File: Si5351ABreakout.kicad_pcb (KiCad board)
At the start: 2 copper layers, 30 x 50 mm, 37 parts, among them J1 Power/Data, J2 SMA-F, J3 SMA-F, J4 SMA-F, J5 CLK0, J6 CLK1, J7 CLK2, T1 TC1-6X+, T2 TC1-6X+, T3 TC1-6X+, U1 Si5351A, X1 ECS-250-8-30B-CKM

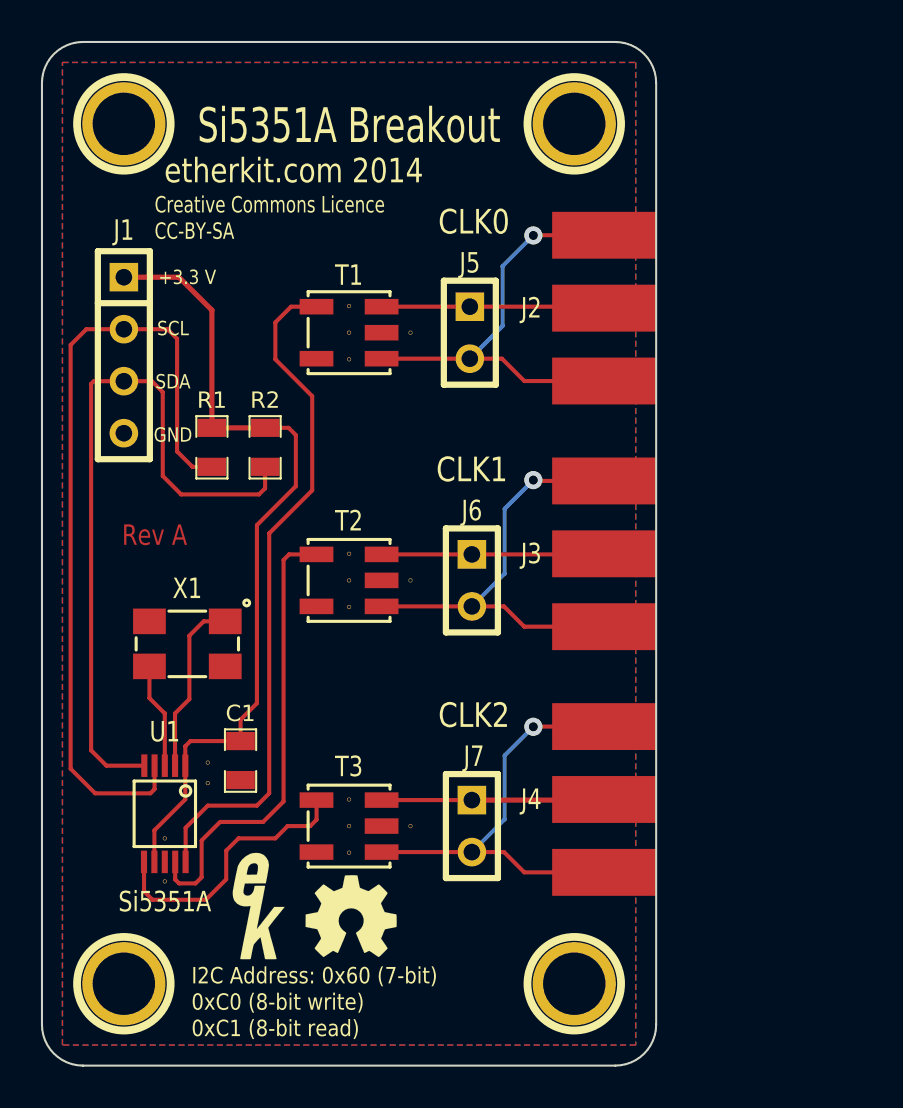
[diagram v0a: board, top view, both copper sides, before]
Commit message: Rev B - I2C level conv, voltage regulator
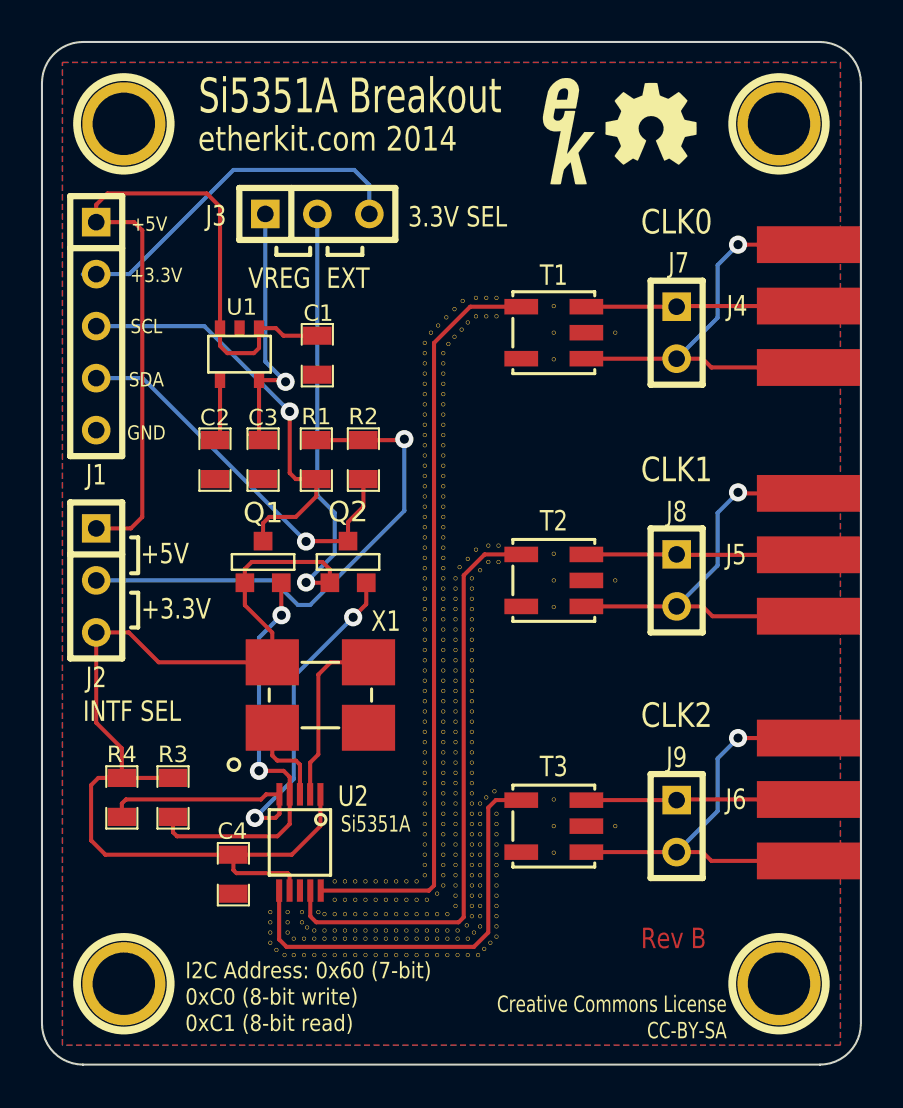
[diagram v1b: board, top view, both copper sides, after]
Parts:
- removed the VIA at (106.0, 91.0)
- added C2: 10n, EtherkitKicadLibrary:SM0805, F.Cu at (108.5, 70.4)
- added C3: 4.7u MLCC, EtherkitKicadLibrary:SM0805, F.Cu at (110.8, 70.4)
- added C4: 100n, EtherkitKicadLibrary:SM0805, F.Cu at (109.3, 90.7)
- added J8: CLK1, EtherkitKicadLibrary:SIL-2, F.Cu at (131.0, 76.3)
- added J9: CLK2, EtherkitKicadLibrary:SIL-2, F.Cu at (131.0, 88.3)
- added Q1: 2N7002, EtherkitKicadLibrary:SOT23-2N7002, F.Cu at (110.8, 75.4)
- added Q2: 2N7002, EtherkitKicadLibrary:SOT23-2N7002, F.Cu at (115.0, 75.4)
- added R3: 10k, EtherkitKicadLibrary:SM0805, F.Cu at (106.4, 86.9)
- added R4: 10k, EtherkitKicadLibrary:SM0805, F.Cu at (103.9, 86.9)
- added U2: Si5351A, EtherkitKicadLibrary:MSOP-10, F.Cu at (112.6, 89.1)
- added VIA: VAL**, EtherkitKicadLibrary:VIA, F.Cu at (114.8, 93.4)
- added VIA: VAL**, EtherkitKicadLibrary:VIA, F.Cu at (115.3, 93.4)
- added VIA: VAL**, EtherkitKicadLibrary:VIA, F.Cu at (115.8, 93.4)
- added VIA: VAL**, EtherkitKicadLibrary:VIA, F.Cu at (116.3, 93.4)
- added VIA: VAL**, EtherkitKicadLibrary:VIA, F.Cu at (116.8, 93.4)
- added VIA: VAL**, EtherkitKicadLibrary:VIA, F.Cu at (117.3, 93.4)
- added VIA: VAL**, EtherkitKicadLibrary:VIA, F.Cu at (117.8, 93.4)
- added VIA: VAL**, EtherkitKicadLibrary:VIA, F.Cu at (118.3, 93.4)
- added VIA: VAL**, EtherkitKicadLibrary:VIA, F.Cu at (118.8, 93.4)
- added VIA: VAL**, EtherkitKicadLibrary:VIA, F.Cu at (119.3, 93.4)
- added VIA: VAL**, EtherkitKicadLibrary:VIA, F.Cu at (119.8, 93.4)
- added VIA: VAL**, EtherkitKicadLibrary:VIA, F.Cu at (120.3, 93.4)
- added VIA: VAL**, EtherkitKicadLibrary:VIA, F.Cu at (121.0, 92.7)
- added VIA: VAL**, EtherkitKicadLibrary:VIA, F.Cu at (120.8, 93.2)
- added VIA: VAL**, EtherkitKicadLibrary:VIA, F.Cu at (121.0, 92.2)
- added VIA: VAL**, EtherkitKicadLibrary:VIA, F.Cu at (121.0, 91.7)
- added VIA: VAL**, EtherkitKicadLibrary:VIA, F.Cu at (121.0, 91.2)
- added VIA: VAL**, EtherkitKicadLibrary:VIA, F.Cu at (121.0, 90.7)
- added VIA: VAL**, EtherkitKicadLibrary:VIA, F.Cu at (121.0, 90.2)
- added VIA: VAL**, EtherkitKicadLibrary:VIA, F.Cu at (121.0, 89.7)
- added VIA: VAL**, EtherkitKicadLibrary:VIA, F.Cu at (121.0, 89.2)
- added VIA: VAL**, EtherkitKicadLibrary:VIA, F.Cu at (121.0, 88.7)
- added VIA: VAL**, EtherkitKicadLibrary:VIA, F.Cu at (121.0, 88.2)
- added VIA: VAL**, EtherkitKicadLibrary:VIA, F.Cu at (121.0, 87.7)
- added VIA: VAL**, EtherkitKicadLibrary:VIA, F.Cu at (121.0, 87.2)
- added VIA: VAL**, EtherkitKicadLibrary:VIA, F.Cu at (121.0, 86.7)
- added VIA: VAL**, EtherkitKicadLibrary:VIA, F.Cu at (121.0, 86.2)
- added VIA: VAL**, EtherkitKicadLibrary:VIA, F.Cu at (121.0, 85.7)
- added VIA: VAL**, EtherkitKicadLibrary:VIA, F.Cu at (121.0, 85.2)
- added VIA: VAL**, EtherkitKicadLibrary:VIA, F.Cu at (121.0, 84.7)
- added VIA: VAL**, EtherkitKicadLibrary:VIA, F.Cu at (121.0, 84.2)
- added VIA: VAL**, EtherkitKicadLibrary:VIA, F.Cu at (121.0, 83.7)
- added VIA: VAL**, EtherkitKicadLibrary:VIA, F.Cu at (121.0, 83.2)
- added VIA: VAL**, EtherkitKicadLibrary:VIA, F.Cu at (121.0, 82.7)
- added VIA: VAL**, EtherkitKicadLibrary:VIA, F.Cu at (121.0, 82.2)
- added VIA: VAL**, EtherkitKicadLibrary:VIA, F.Cu at (121.0, 81.7)
- added VIA: VAL**, EtherkitKicadLibrary:VIA, F.Cu at (121.0, 81.2)
- added VIA: VAL**, EtherkitKicadLibrary:VIA, F.Cu at (121.0, 80.7)
- added VIA: VAL**, EtherkitKicadLibrary:VIA, F.Cu at (121.0, 80.2)
- added VIA: VAL**, EtherkitKicadLibrary:VIA, F.Cu at (121.0, 79.7)
- added VIA: VAL**, EtherkitKicadLibrary:VIA, F.Cu at (121.0, 79.2)
- added VIA: VAL**, EtherkitKicadLibrary:VIA, F.Cu at (121.0, 78.7)
- added VIA: VAL**, EtherkitKicadLibrary:VIA, F.Cu at (121.0, 78.2)
- added VIA: VAL**, EtherkitKicadLibrary:VIA, F.Cu at (121.0, 77.7)
- added VIA: VAL**, EtherkitKicadLibrary:VIA, F.Cu at (121.0, 77.2)
- added VIA: VAL**, EtherkitKicadLibrary:VIA, F.Cu at (121.0, 76.7)
- added VIA: VAL**, EtherkitKicadLibrary:VIA, F.Cu at (121.0, 76.2)
- added VIA: VAL**, EtherkitKicadLibrary:VIA, F.Cu at (121.8, 75.4)
- added VIA: VAL**, EtherkitKicadLibrary:VIA, F.Cu at (122.3, 75.4)
- added VIA: VAL**, EtherkitKicadLibrary:VIA, F.Cu at (121.4, 75.8)
- added VIA: VAL**, EtherkitKicadLibrary:VIA, F.Cu at (114.3, 92.6)
- added VIA: VAL**, EtherkitKicadLibrary:VIA, F.Cu at (114.8, 92.6)
- added VIA: VAL**, EtherkitKicadLibrary:VIA, F.Cu at (115.3, 92.6)
- added VIA: VAL**, EtherkitKicadLibrary:VIA, F.Cu at (115.8, 92.6)
- added VIA: VAL**, EtherkitKicadLibrary:VIA, F.Cu at (116.3, 92.6)
- added VIA: VAL**, EtherkitKicadLibrary:VIA, F.Cu at (116.8, 92.6)
- added VIA: VAL**, EtherkitKicadLibrary:VIA, F.Cu at (117.3, 92.6)
- added VIA: VAL**, EtherkitKicadLibrary:VIA, F.Cu at (117.8, 92.6)
- added VIA: VAL**, EtherkitKicadLibrary:VIA, F.Cu at (118.3, 92.6)
- added VIA: VAL**, EtherkitKicadLibrary:VIA, F.Cu at (118.8, 92.6)
- added VIA: VAL**, EtherkitKicadLibrary:VIA, F.Cu at (112.0, 92.5)
- added VIA: VAL**, EtherkitKicadLibrary:VIA, F.Cu at (119.3, 92.6)
- added VIA: VAL**, EtherkitKicadLibrary:VIA, F.Cu at (119.8, 92.6)
- added VIA: VAL**, EtherkitKicadLibrary:VIA, F.Cu at (120.2, 92.2)
- added VIA: VAL**, EtherkitKicadLibrary:VIA, F.Cu at (120.2, 91.7)
- added VIA: VAL**, EtherkitKicadLibrary:VIA, F.Cu at (120.2, 91.2)
- added VIA: VAL**, EtherkitKicadLibrary:VIA, F.Cu at (120.2, 90.7)
- added VIA: VAL**, EtherkitKicadLibrary:VIA, F.Cu at (120.2, 90.2)
- added VIA: VAL**, EtherkitKicadLibrary:VIA, F.Cu at (120.2, 89.7)
- added VIA: VAL**, EtherkitKicadLibrary:VIA, F.Cu at (120.2, 89.2)
- added VIA: VAL**, EtherkitKicadLibrary:VIA, F.Cu at (120.2, 88.7)
- added VIA: VAL**, EtherkitKicadLibrary:VIA, F.Cu at (112.0, 93.0)
- added VIA: VAL**, EtherkitKicadLibrary:VIA, F.Cu at (120.2, 88.2)
- added VIA: VAL**, EtherkitKicadLibrary:VIA, F.Cu at (120.2, 87.7)
- added VIA: VAL**, EtherkitKicadLibrary:VIA, F.Cu at (120.2, 87.2)
- added VIA: VAL**, EtherkitKicadLibrary:VIA, F.Cu at (120.2, 86.7)
- added VIA: VAL**, EtherkitKicadLibrary:VIA, F.Cu at (120.2, 86.2)
- added VIA: VAL**, EtherkitKicadLibrary:VIA, F.Cu at (120.2, 85.7)
- added VIA: VAL**, EtherkitKicadLibrary:VIA, F.Cu at (120.2, 85.2)
- added VIA: VAL**, EtherkitKicadLibrary:VIA, F.Cu at (120.2, 84.7)
- added VIA: VAL**, EtherkitKicadLibrary:VIA, F.Cu at (120.2, 84.2)
- added VIA: VAL**, EtherkitKicadLibrary:VIA, F.Cu at (120.2, 83.7)
- added VIA: VAL**, EtherkitKicadLibrary:VIA, F.Cu at (111.2, 93.0)
- added VIA: VAL**, EtherkitKicadLibrary:VIA, F.Cu at (120.2, 83.2)
- added VIA: VAL**, EtherkitKicadLibrary:VIA, F.Cu at (120.2, 82.7)
- added VIA: VAL**, EtherkitKicadLibrary:VIA, F.Cu at (120.2, 82.2)
- added VIA: VAL**, EtherkitKicadLibrary:VIA, F.Cu at (120.2, 81.7)
- added VIA: VAL**, EtherkitKicadLibrary:VIA, F.Cu at (120.2, 81.2)
- added VIA: VAL**, EtherkitKicadLibrary:VIA, F.Cu at (120.2, 80.7)
- added VIA: VAL**, EtherkitKicadLibrary:VIA, F.Cu at (120.2, 80.2)
- added VIA: VAL**, EtherkitKicadLibrary:VIA, F.Cu at (120.2, 79.7)
- added VIA: VAL**, EtherkitKicadLibrary:VIA, F.Cu at (120.2, 79.2)
- added VIA: VAL**, EtherkitKicadLibrary:VIA, F.Cu at (120.2, 78.7)
- added VIA: VAL**, EtherkitKicadLibrary:VIA, F.Cu at (112.0, 93.5)
- added VIA: VAL**, EtherkitKicadLibrary:VIA, F.Cu at (120.2, 78.2)
- added VIA: VAL**, EtherkitKicadLibrary:VIA, F.Cu at (120.2, 77.7)
- added VIA: VAL**, EtherkitKicadLibrary:VIA, F.Cu at (120.2, 77.2)
- added VIA: VAL**, EtherkitKicadLibrary:VIA, F.Cu at (120.2, 76.7)
- added VIA: VAL**, EtherkitKicadLibrary:VIA, F.Cu at (120.2, 76.2)
- added VIA: VAL**, EtherkitKicadLibrary:VIA, F.Cu at (121.8, 74.6)
- added VIA: VAL**, EtherkitKicadLibrary:VIA, F.Cu at (122.3, 74.6)
- added VIA: VAL**, EtherkitKicadLibrary:VIA, F.Cu at (120.4, 75.7)
- added VIA: VAL**, EtherkitKicadLibrary:VIA, F.Cu at (121.2, 74.8)
- added VIA: VAL**, EtherkitKicadLibrary:VIA, F.Cu at (120.8, 75.2)
- added VIA: VAL**, EtherkitKicadLibrary:VIA, F.Cu at (111.2, 93.5)
- added VIA: VAL**, EtherkitKicadLibrary:VIA, F.Cu at (114.3, 91.9)
- added VIA: VAL**, EtherkitKicadLibrary:VIA, F.Cu at (114.3, 91.0)
- added VIA: VAL**, EtherkitKicadLibrary:VIA, F.Cu at (114.8, 91.9)
- added VIA: VAL**, EtherkitKicadLibrary:VIA, F.Cu at (115.3, 91.9)
- added VIA: VAL**, EtherkitKicadLibrary:VIA, F.Cu at (115.8, 91.9)
- added VIA: VAL**, EtherkitKicadLibrary:VIA, F.Cu at (116.3, 91.9)
- added VIA: VAL**, EtherkitKicadLibrary:VIA, F.Cu at (116.8, 91.9)
- added VIA: VAL**, EtherkitKicadLibrary:VIA, F.Cu at (117.3, 91.9)
- added VIA: VAL**, EtherkitKicadLibrary:VIA, F.Cu at (117.8, 91.9)
- added VIA: VAL**, EtherkitKicadLibrary:VIA, F.Cu at (118.3, 91.9)
- added VIA: VAL**, EtherkitKicadLibrary:VIA, F.Cu at (111.5, 94.3)
- added VIA: VAL**, EtherkitKicadLibrary:VIA, F.Cu at (118.8, 91.9)
- added VIA: VAL**, EtherkitKicadLibrary:VIA, F.Cu at (119.6, 90.7)
- added VIA: VAL**, EtherkitKicadLibrary:VIA, F.Cu at (114.8, 91.0)
- added VIA: VAL**, EtherkitKicadLibrary:VIA, F.Cu at (115.3, 91.0)
- added VIA: VAL**, EtherkitKicadLibrary:VIA, F.Cu at (115.8, 91.0)
- added VIA: VAL**, EtherkitKicadLibrary:VIA, F.Cu at (116.3, 91.0)
- added VIA: VAL**, EtherkitKicadLibrary:VIA, F.Cu at (116.8, 91.0)
- added VIA: VAL**, EtherkitKicadLibrary:VIA, F.Cu at (117.3, 91.0)
- added VIA: VAL**, EtherkitKicadLibrary:VIA, F.Cu at (117.8, 91.0)
- added VIA: VAL**, EtherkitKicadLibrary:VIA, F.Cu at (118.3, 91.0)
- added VIA: VAL**, EtherkitKicadLibrary:VIA, F.Cu at (112.3, 93.8)
- added VIA: VAL**, EtherkitKicadLibrary:VIA, F.Cu at (118.7, 90.7)
- added VIA: VAL**, EtherkitKicadLibrary:VIA, F.Cu at (119.6, 91.2)
- added VIA: VAL**, EtherkitKicadLibrary:VIA, F.Cu at (119.3, 91.6)
- added VIA: VAL**, EtherkitKicadLibrary:VIA, F.Cu at (119.6, 90.2)
- added VIA: VAL**, EtherkitKicadLibrary:VIA, F.Cu at (119.6, 89.7)
- added VIA: VAL**, EtherkitKicadLibrary:VIA, F.Cu at (119.6, 89.2)
- added VIA: VAL**, EtherkitKicadLibrary:VIA, F.Cu at (119.6, 88.7)
- added VIA: VAL**, EtherkitKicadLibrary:VIA, F.Cu at (119.6, 88.2)
- added VIA: VAL**, EtherkitKicadLibrary:VIA, F.Cu at (119.6, 87.7)
- added VIA: VAL**, EtherkitKicadLibrary:VIA, F.Cu at (119.6, 87.2)
- added VIA: VAL**, EtherkitKicadLibrary:VIA, F.Cu at (112.8, 94.6)
- added VIA: VAL**, EtherkitKicadLibrary:VIA, F.Cu at (119.6, 86.7)
- added VIA: VAL**, EtherkitKicadLibrary:VIA, F.Cu at (119.6, 86.2)
- added VIA: VAL**, EtherkitKicadLibrary:VIA, F.Cu at (119.6, 85.7)
- added VIA: VAL**, EtherkitKicadLibrary:VIA, F.Cu at (119.6, 85.2)
- added VIA: VAL**, EtherkitKicadLibrary:VIA, F.Cu at (119.6, 84.7)
- added VIA: VAL**, EtherkitKicadLibrary:VIA, F.Cu at (119.6, 84.2)
- added VIA: VAL**, EtherkitKicadLibrary:VIA, F.Cu at (119.6, 83.7)
- added VIA: VAL**, EtherkitKicadLibrary:VIA, F.Cu at (119.6, 83.2)
- added VIA: VAL**, EtherkitKicadLibrary:VIA, F.Cu at (119.6, 82.7)
- added VIA: VAL**, EtherkitKicadLibrary:VIA, F.Cu at (119.6, 82.2)
- added VIA: VAL**, EtherkitKicadLibrary:VIA, F.Cu at (112.3, 94.6)
- added VIA: VAL**, EtherkitKicadLibrary:VIA, F.Cu at (119.6, 81.7)
- added VIA: VAL**, EtherkitKicadLibrary:VIA, F.Cu at (119.6, 81.2)
- added VIA: VAL**, EtherkitKicadLibrary:VIA, F.Cu at (119.6, 80.7)
- added VIA: VAL**, EtherkitKicadLibrary:VIA, F.Cu at (119.6, 80.2)
- added VIA: VAL**, EtherkitKicadLibrary:VIA, F.Cu at (119.6, 79.7)
- added VIA: VAL**, EtherkitKicadLibrary:VIA, F.Cu at (119.6, 79.2)
- added VIA: VAL**, EtherkitKicadLibrary:VIA, F.Cu at (119.6, 78.7)
- added VIA: VAL**, EtherkitKicadLibrary:VIA, F.Cu at (119.6, 78.2)
- added VIA: VAL**, EtherkitKicadLibrary:VIA, F.Cu at (119.6, 77.7)
- added VIA: VAL**, EtherkitKicadLibrary:VIA, F.Cu at (119.6, 77.2)
- added VIA: VAL**, EtherkitKicadLibrary:VIA, F.Cu at (111.2, 94.0)
- added VIA: VAL**, EtherkitKicadLibrary:VIA, F.Cu at (119.6, 76.7)
- added VIA: VAL**, EtherkitKicadLibrary:VIA, F.Cu at (119.6, 76.2)
- added VIA: VAL**, EtherkitKicadLibrary:VIA, F.Cu at (119.6, 75.7)
- added VIA: VAL**, EtherkitKicadLibrary:VIA, F.Cu at (119.6, 75.2)
- added VIA: VAL**, EtherkitKicadLibrary:VIA, F.Cu at (119.6, 74.7)
- added VIA: VAL**, EtherkitKicadLibrary:VIA, F.Cu at (119.6, 74.2)
- added VIA: VAL**, EtherkitKicadLibrary:VIA, F.Cu at (119.6, 73.7)
- added VIA: VAL**, EtherkitKicadLibrary:VIA, F.Cu at (119.6, 73.2)
- added VIA: VAL**, EtherkitKicadLibrary:VIA, F.Cu at (119.6, 72.7)
- added VIA: VAL**, EtherkitKicadLibrary:VIA, F.Cu at (119.6, 72.2)
- added VIA: VAL**, EtherkitKicadLibrary:VIA, F.Cu at (111.8, 94.6)
- added VIA: VAL**, EtherkitKicadLibrary:VIA, F.Cu at (119.6, 71.7)
- added VIA: VAL**, EtherkitKicadLibrary:VIA, F.Cu at (119.6, 71.2)
- added VIA: VAL**, EtherkitKicadLibrary:VIA, F.Cu at (119.6, 70.7)
- added VIA: VAL**, EtherkitKicadLibrary:VIA, F.Cu at (119.6, 70.2)
- added VIA: VAL**, EtherkitKicadLibrary:VIA, F.Cu at (119.6, 69.7)
- added VIA: VAL**, EtherkitKicadLibrary:VIA, F.Cu at (119.6, 69.2)
- added VIA: VAL**, EtherkitKicadLibrary:VIA, F.Cu at (119.6, 68.7)
- added VIA: VAL**, EtherkitKicadLibrary:VIA, F.Cu at (119.6, 68.2)
- added VIA: VAL**, EtherkitKicadLibrary:VIA, F.Cu at (119.6, 67.7)
- added VIA: VAL**, EtherkitKicadLibrary:VIA, F.Cu at (119.6, 67.2)
- added VIA: VAL**, EtherkitKicadLibrary:VIA, F.Cu at (112.8, 93.8)
- added VIA: VAL**, EtherkitKicadLibrary:VIA, F.Cu at (119.6, 66.7)
- added VIA: VAL**, EtherkitKicadLibrary:VIA, F.Cu at (119.6, 66.2)
- added VIA: VAL**, EtherkitKicadLibrary:VIA, F.Cu at (119.6, 65.7)
- added VIA: VAL**, EtherkitKicadLibrary:VIA, F.Cu at (119.6, 65.2)
- added VIA: VAL**, EtherkitKicadLibrary:VIA, F.Cu at (121.2, 63.4)
- added VIA: VAL**, EtherkitKicadLibrary:VIA, F.Cu at (121.7, 63.4)
- added VIA: VAL**, EtherkitKicadLibrary:VIA, F.Cu at (122.2, 63.4)
- added VIA: VAL**, EtherkitKicadLibrary:VIA, F.Cu at (119.8, 64.8)
- added VIA: VAL**, EtherkitKicadLibrary:VIA, F.Cu at (120.2, 64.4)
- added VIA: VAL**, EtherkitKicadLibrary:VIA, F.Cu at (120.5, 64.0)
- added VIA: VAL**, EtherkitKicadLibrary:VIA, F.Cu at (113.3, 93.8)
- added VIA: VAL**, EtherkitKicadLibrary:VIA, F.Cu at (120.8, 63.7)
- added VIA: VAL**, EtherkitKicadLibrary:VIA, F.Cu at (118.7, 90.2)
- added VIA: VAL**, EtherkitKicadLibrary:VIA, F.Cu at (118.7, 89.7)
- added VIA: VAL**, EtherkitKicadLibrary:VIA, F.Cu at (118.7, 89.2)
- added VIA: VAL**, EtherkitKicadLibrary:VIA, F.Cu at (118.7, 88.7)
- added VIA: VAL**, EtherkitKicadLibrary:VIA, F.Cu at (118.7, 88.2)
- added VIA: VAL**, EtherkitKicadLibrary:VIA, F.Cu at (118.7, 87.7)
- added VIA: VAL**, EtherkitKicadLibrary:VIA, F.Cu at (118.7, 87.2)
- added VIA: VAL**, EtherkitKicadLibrary:VIA, F.Cu at (118.7, 86.7)
- added VIA: VAL**, EtherkitKicadLibrary:VIA, F.Cu at (118.7, 86.2)
- added VIA: VAL**, EtherkitKicadLibrary:VIA, F.Cu at (113.8, 93.8)
- added VIA: VAL**, EtherkitKicadLibrary:VIA, F.Cu at (118.7, 85.7)
- added VIA: VAL**, EtherkitKicadLibrary:VIA, F.Cu at (118.7, 85.2)
- added VIA: VAL**, EtherkitKicadLibrary:VIA, F.Cu at (118.7, 84.7)
- added VIA: VAL**, EtherkitKicadLibrary:VIA, F.Cu at (118.7, 84.2)
- added VIA: VAL**, EtherkitKicadLibrary:VIA, F.Cu at (118.7, 83.7)
- added VIA: VAL**, EtherkitKicadLibrary:VIA, F.Cu at (118.7, 83.2)
- added VIA: VAL**, EtherkitKicadLibrary:VIA, F.Cu at (118.7, 82.7)
- added VIA: VAL**, EtherkitKicadLibrary:VIA, F.Cu at (118.7, 82.2)
- added VIA: VAL**, EtherkitKicadLibrary:VIA, F.Cu at (118.7, 81.7)
- added VIA: VAL**, EtherkitKicadLibrary:VIA, F.Cu at (118.7, 81.2)
- added VIA: VAL**, EtherkitKicadLibrary:VIA, F.Cu at (114.3, 93.8)
- added VIA: VAL**, EtherkitKicadLibrary:VIA, F.Cu at (118.7, 80.7)
- added VIA: VAL**, EtherkitKicadLibrary:VIA, F.Cu at (118.7, 80.2)
- added VIA: VAL**, EtherkitKicadLibrary:VIA, F.Cu at (118.7, 79.7)
- added VIA: VAL**, EtherkitKicadLibrary:VIA, F.Cu at (118.7, 79.2)
- added VIA: VAL**, EtherkitKicadLibrary:VIA, F.Cu at (118.7, 78.7)
- added VIA: VAL**, EtherkitKicadLibrary:VIA, F.Cu at (118.7, 78.2)
- added VIA: VAL**, EtherkitKicadLibrary:VIA, F.Cu at (118.7, 77.7)
- added VIA: VAL**, EtherkitKicadLibrary:VIA, F.Cu at (118.7, 77.2)
- added VIA: VAL**, EtherkitKicadLibrary:VIA, F.Cu at (118.7, 76.7)
- added VIA: VAL**, EtherkitKicadLibrary:VIA, F.Cu at (118.7, 76.2)
- added VIA: VAL**, EtherkitKicadLibrary:VIA, F.Cu at (114.8, 93.8)
- added VIA: VAL**, EtherkitKicadLibrary:VIA, F.Cu at (118.7, 75.7)
- added VIA: VAL**, EtherkitKicadLibrary:VIA, F.Cu at (118.7, 75.2)
- added VIA: VAL**, EtherkitKicadLibrary:VIA, F.Cu at (118.7, 74.7)
- added VIA: VAL**, EtherkitKicadLibrary:VIA, F.Cu at (118.7, 74.2)
- added VIA: VAL**, EtherkitKicadLibrary:VIA, F.Cu at (118.7, 73.7)
- added VIA: VAL**, EtherkitKicadLibrary:VIA, F.Cu at (118.7, 73.2)
- added VIA: VAL**, EtherkitKicadLibrary:VIA, F.Cu at (118.7, 72.7)
- added VIA: VAL**, EtherkitKicadLibrary:VIA, F.Cu at (118.7, 72.2)
- added VIA: VAL**, EtherkitKicadLibrary:VIA, F.Cu at (118.7, 71.7)
- added VIA: VAL**, EtherkitKicadLibrary:VIA, F.Cu at (118.7, 71.2)
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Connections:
- C1 pad 1: +3.3V -> +5V
- J1 pad 1: +3.3V -> +5V
- J1 pad 2: Net-(J1-Pad2) -> +3.3V
- J1 pad 4: GND -> Net-(J1-Pad4)
- J2 pad 1: Net-(J2-Pad1) -> +5V
- J3 pad 1: Net-(J3-Pad1) -> Net-(C3-Pad1)
- J3 pad 2: Net-(J3-Pad2) -> +3.3VREG
- J5 pad 1: Net-(J2-Pad1) -> Net-(J5-Pad1)
- J5 pad 2: Net-(J2-Pad2) -> Net-(J5-Pad2)
- J6 pad 1: Net-(J3-Pad1) -> Net-(J6-Pad1)
- J6 pad 2: Net-(J3-Pad2) -> Net-(J6-Pad2)
- R1 pad 1: +3.3V -> Net-(J2-Pad2)
- R1 pad 2: Net-(J1-Pad2) -> Net-(J1-Pad3)
- R2 pad 1: +3.3V -> Net-(J2-Pad2)
- R2 pad 2: Net-(J1-Pad3) -> Net-(J1-Pad4)
- T1 pad 1: Net-(J2-Pad1) -> Net-(J4-Pad1)
- T1 pad 2: GND -> (no net)
- T1 pad 3: Net-(J2-Pad2) -> Net-(J4-Pad2)
- T2 pad 1: Net-(J3-Pad1) -> Net-(J5-Pad1)
- T2 pad 2: GND -> (no net)
- T2 pad 3: Net-(J3-Pad2) -> Net-(J5-Pad2)
- T3 pad 1: Net-(J4-Pad1) -> Net-(J6-Pad1)
- T3 pad 2: GND -> (no net)
- T3 pad 3: Net-(J4-Pad2) -> Net-(J6-Pad2)
- U1 pad 1: +3.3V -> +5V
- U1 pad 2: Net-(U1-Pad2) -> GND
- U1 pad 3: Net-(U1-Pad3) -> +5V
- U1 pad 4: Net-(J1-Pad2) -> Net-(C2-Pad1)
- U1 pad 5: Net-(J1-Pad3) -> Net-(C3-Pad1)
- X1 pad 1: Net-(U1-Pad2) -> Net-(U2-Pad3)
- X1 pad 2: (no net) -> GND
- X1 pad 3: Net-(U1-Pad3) -> Net-(U2-Pad2)
- X1 pad 4: (no net) -> +3.3VREG
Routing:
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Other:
- board size 30 x 50 mm -> 40 x 50 mm
- net class Default: clearance 0.2 -> 0.15
- rule trace_clearance: 0.2 -> 0.15
- board text added: "+3.3V"
- board text added: "+5V"
- board text added: "3.3V SEL"
- board text added: "Creative Commons License CC-BY-SA"
- board text added: "EXT"
- board text added: "INTF SEL"
- board text added: "Rev B"
- board text added: "VREG"
- board text removed: "+3.3 V"
- board text removed: "Creative Commons Licence CC-BY-SA"
- board text removed: "Rev A"

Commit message: Rev C updates
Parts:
- removed T1, T2, T3: Mini-Circuits TC1-6X+, EtherkitKicadLibrary:TC1-6X+
- removed the VIA at (111.2, 92.5)
- removed the VIA at (125.0, 75.0)
- removed the VIA at (114.8, 93.4)
- removed the VIA at (115.3, 93.4)
- removed the VIA at (115.8, 93.4)
- removed the VIA at (116.3, 93.4)
- removed the VIA at (116.8, 93.4)
- removed the VIA at (117.3, 93.4)
- removed the VIA at (117.8, 93.4)
- removed the VIA at (118.3, 93.4)
- removed the VIA at (118.8, 93.4)
- removed the VIA at (119.3, 93.4)
- removed the VIA at (125.0, 77.6)
- removed the VIA at (119.8, 93.4)
- removed the VIA at (120.3, 93.4)
- removed the VIA at (121.0, 92.7)
- removed the VIA at (120.8, 93.2)
- removed the VIA at (121.0, 92.2)
- removed the VIA at (121.0, 91.7)
- removed the VIA at (121.0, 91.2)
- removed the VIA at (121.0, 90.7)
- removed the VIA at (121.0, 90.2)
- removed the VIA at (121.0, 89.7)
- removed the VIA at (128.0, 64.2)
- removed the VIA at (121.0, 89.2)
- removed the VIA at (121.0, 88.7)
- removed the VIA at (121.0, 88.2)
- removed the VIA at (121.0, 87.7)
- removed the VIA at (121.0, 87.2)
- removed the VIA at (121.0, 86.7)
- removed the VIA at (121.0, 86.2)
- removed the VIA at (121.0, 85.7)
- removed the VIA at (121.0, 85.2)
- removed the VIA at (121.0, 84.7)
- removed the VIA at (125.0, 64.2)
- removed the VIA at (121.0, 84.2)
- removed the VIA at (121.0, 83.7)
- removed the VIA at (121.0, 83.2)
- removed the VIA at (121.0, 82.7)
- removed the VIA at (121.0, 82.2)
- removed the VIA at (121.0, 81.7)
- removed the VIA at (121.0, 81.2)
- removed the VIA at (121.0, 80.7)
- removed the VIA at (121.0, 80.2)
- removed the VIA at (121.0, 79.7)
- removed the VIA at (125.0, 65.5)
- removed the VIA at (121.0, 79.2)
- removed the VIA at (121.0, 78.7)
- removed the VIA at (121.0, 78.2)
- removed the VIA at (121.0, 77.7)
- removed the VIA at (121.0, 77.2)
- removed the VIA at (121.0, 76.7)
- removed the VIA at (121.0, 76.2)
- removed the VIA at (121.8, 75.4)
- removed the VIA at (122.3, 75.4)
- removed the VIA at (121.4, 75.8)
- removed the VIA at (125.0, 62.9)
- removed the VIA at (114.3, 92.6)
- removed the VIA at (114.8, 92.6)
- removed the VIA at (115.3, 92.6)
- removed the VIA at (115.8, 92.6)
- removed the VIA at (116.3, 92.6)
- removed the VIA at (116.8, 92.6)
- removed the VIA at (117.3, 92.6)
- removed the VIA at (117.8, 92.6)
- removed the VIA at (118.3, 92.6)
- removed the VIA at (118.8, 92.6)
- removed the VIA at (112.0, 92.5)
- removed the VIA at (119.3, 92.6)
- removed the VIA at (119.8, 92.6)
- removed the VIA at (120.2, 92.2)
- removed the VIA at (120.2, 91.7)
- removed the VIA at (120.2, 91.2)
- removed the VIA at (120.2, 90.7)
- removed the VIA at (120.2, 90.2)
- removed the VIA at (120.2, 89.7)
- removed the VIA at (120.2, 89.2)
- removed the VIA at (120.2, 88.7)
- removed the VIA at (112.0, 93.0)
- removed the VIA at (120.2, 88.2)
- removed the VIA at (120.2, 87.7)
- removed the VIA at (120.2, 87.2)
- removed the VIA at (120.2, 86.7)
- removed the VIA at (120.2, 86.2)
- removed the VIA at (120.2, 85.7)
- removed the VIA at (120.2, 85.2)
- removed the VIA at (120.2, 84.7)
- removed the VIA at (120.2, 84.2)
- removed the VIA at (120.2, 83.7)
- removed the VIA at (111.2, 93.0)
- removed the VIA at (120.2, 83.2)
- removed the VIA at (120.2, 82.7)
- removed the VIA at (120.2, 82.2)
- removed the VIA at (120.2, 81.7)
- removed the VIA at (120.2, 81.2)
- removed the VIA at (120.2, 80.7)
- removed the VIA at (120.2, 80.2)
- removed the VIA at (120.2, 79.7)
- removed the VIA at (120.2, 79.2)
- removed the VIA at (120.2, 78.7)
- removed the VIA at (112.0, 93.5)
- removed the VIA at (120.2, 78.2)
- removed the VIA at (120.2, 77.7)
- removed the VIA at (120.2, 77.2)
- removed the VIA at (120.2, 76.7)
- removed the VIA at (120.2, 76.2)
- removed the VIA at (121.8, 74.6)
- removed the VIA at (122.3, 74.6)
- removed the VIA at (120.4, 75.7)
- removed the VIA at (121.2, 74.8)
- removed the VIA at (120.8, 75.2)
- removed the VIA at (111.2, 93.5)
- removed the VIA at (114.8, 91.9)
- removed the VIA at (115.3, 91.9)
- removed the VIA at (115.8, 91.9)
- removed the VIA at (116.3, 91.9)
- removed the VIA at (116.8, 91.9)
- removed the VIA at (117.3, 91.9)
- removed the VIA at (117.8, 91.9)
- removed the VIA at (118.3, 91.9)
- removed the VIA at (111.5, 94.3)
- removed the VIA at (118.8, 91.9)
- removed the VIA at (119.6, 90.7)
- removed the VIA at (114.8, 91.0)
- removed the VIA at (115.3, 91.0)
- removed the VIA at (115.8, 91.0)
- removed the VIA at (116.3, 91.0)
- removed the VIA at (116.8, 91.0)
- removed the VIA at (117.3, 91.0)
- removed the VIA at (117.8, 91.0)
- removed the VIA at (118.3, 91.0)
- removed the VIA at (112.3, 93.8)
- removed the VIA at (118.7, 90.7)
- removed the VIA at (119.6, 91.2)
- removed the VIA at (119.3, 91.6)
- removed the VIA at (119.6, 90.2)
- removed the VIA at (119.6, 89.7)
- removed the VIA at (119.6, 89.2)
- removed the VIA at (119.6, 88.7)
- removed the VIA at (119.6, 88.2)
- removed the VIA at (119.6, 87.7)
- removed the VIA at (119.6, 87.2)
- removed the VIA at (112.8, 94.6)
- removed the VIA at (119.6, 86.7)
- removed the VIA at (119.6, 86.2)
- removed the VIA at (119.6, 85.7)
- removed the VIA at (119.6, 85.2)
- removed the VIA at (119.6, 84.7)
- removed the VIA at (119.6, 84.2)
- removed the VIA at (119.6, 83.7)
- removed the VIA at (119.6, 83.2)
- removed the VIA at (119.6, 82.7)
- removed the VIA at (119.6, 82.2)
- removed the VIA at (112.3, 94.6)
- removed the VIA at (119.6, 81.7)
- removed the VIA at (119.6, 81.2)
- removed the VIA at (119.6, 80.7)
- removed the VIA at (119.6, 80.2)
- removed the VIA at (119.6, 79.7)
- removed the VIA at (119.6, 79.2)
- removed the VIA at (119.6, 78.7)
- removed the VIA at (119.6, 78.2)
- removed the VIA at (119.6, 77.7)
- removed the VIA at (119.6, 77.2)
- removed the VIA at (111.2, 94.0)
- removed the VIA at (119.6, 76.7)
- removed the VIA at (119.6, 76.2)
- removed the VIA at (119.6, 75.7)
- removed the VIA at (119.6, 75.2)
- removed the VIA at (119.6, 74.7)
- removed the VIA at (119.6, 74.2)
- removed the VIA at (119.6, 73.7)
- removed the VIA at (119.6, 73.2)
- removed the VIA at (119.6, 72.7)
- removed the VIA at (119.6, 72.2)
- removed the VIA at (111.8, 94.6)
- removed the VIA at (119.6, 71.7)
- removed the VIA at (119.6, 71.2)
- removed the VIA at (119.6, 70.7)
- removed the VIA at (119.6, 70.2)
- removed the VIA at (119.6, 69.7)
- removed the VIA at (119.6, 69.2)
- removed the VIA at (119.6, 68.7)
- removed the VIA at (119.6, 68.2)
- removed the VIA at (119.6, 67.7)
- removed the VIA at (119.6, 67.2)
- removed the VIA at (112.8, 93.8)
- removed the VIA at (119.6, 66.7)
- removed the VIA at (119.6, 66.2)
- removed the VIA at (119.6, 65.7)
- removed the VIA at (119.6, 65.2)
- removed the VIA at (121.2, 63.4)
- removed the VIA at (121.7, 63.4)
- removed the VIA at (122.2, 63.4)
- removed the VIA at (119.8, 64.8)
- removed the VIA at (120.2, 64.4)
- removed the VIA at (120.5, 64.0)
- removed the VIA at (113.3, 93.8)
- removed the VIA at (120.8, 63.7)
- removed the VIA at (118.7, 90.2)
- removed the VIA at (118.7, 89.7)
- removed the VIA at (118.7, 89.2)
- removed the VIA at (118.7, 88.7)
- removed the VIA at (118.7, 88.2)
- removed the VIA at (118.7, 87.7)
- removed the VIA at (118.7, 87.2)
- removed the VIA at (118.7, 86.7)
- removed the VIA at (118.7, 86.2)
- removed the VIA at (113.8, 93.8)
- removed the VIA at (118.7, 85.7)
- removed the VIA at (118.7, 85.2)
- removed the VIA at (118.7, 84.7)
- removed the VIA at (118.7, 84.2)
- removed the VIA at (118.7, 83.7)
- removed the VIA at (118.7, 83.2)
- removed the VIA at (118.7, 82.7)
- removed the VIA at (118.7, 82.2)
- removed the VIA at (118.7, 81.7)
- removed the VIA at (118.7, 81.2)
- removed the VIA at (128.0, 88.3)
- removed the VIA at (114.3, 93.8)
- removed the VIA at (118.7, 80.7)
- removed the VIA at (118.7, 80.2)
- removed the VIA at (118.7, 79.7)
- removed the VIA at (118.7, 79.2)
- removed the VIA at (118.7, 78.7)
- removed the VIA at (118.7, 78.2)
- removed the VIA at (118.7, 77.7)
- removed the VIA at (118.7, 77.2)
- removed the VIA at (118.7, 76.7)
- removed the VIA at (118.7, 76.2)
- removed the VIA at (114.8, 93.8)
- removed the VIA at (118.7, 75.7)
- removed the VIA at (118.7, 75.2)
- removed the VIA at (118.7, 74.7)
- removed the VIA at (118.7, 74.2)
- removed the VIA at (118.7, 73.7)
- removed the VIA at (118.7, 73.2)
- removed the VIA at (118.7, 72.7)
- removed the VIA at (118.7, 72.2)
- removed the VIA at (118.7, 71.7)
- removed the VIA at (118.7, 71.2)
- removed the VIA at (115.3, 93.8)
- removed the VIA at (118.7, 70.7)
- removed the VIA at (118.7, 70.2)
- removed the VIA at (118.7, 69.7)
- removed the VIA at (118.7, 69.2)
- removed the VIA at (118.7, 68.7)
- removed the VIA at (118.7, 68.2)
- removed the VIA at (118.7, 67.7)
- removed the VIA at (118.7, 67.2)
- removed the VIA at (118.7, 66.7)
- removed the VIA at (118.7, 66.2)
- removed the VIA at (113.8, 93.4)
- removed the VIA at (118.7, 65.7)
- removed the VIA at (118.7, 65.2)
- removed the VIA at (118.7, 64.7)
- removed the VIA at (121.2, 62.5)
- removed the VIA at (121.7, 62.5)
- removed the VIA at (122.2, 62.5)
- removed the VIA at (119.0, 64.2)
- removed the VIA at (119.3, 63.9)
- removed the VIA at (119.8, 63.5)
- removed the VIA at (120.2, 63.0)
- removed the VIA at (114.3, 93.4)
- removed the VIA at (120.5, 62.6)
- removed the VIA at (113.3, 93.4)
- removed the VIA at (115.8, 93.8)
- removed the VIA at (116.3, 93.8)
- removed the VIA at (116.8, 93.8)
- removed the VIA at (117.3, 93.8)
- removed the VIA at (125.0, 88.3)
- removed the VIA at (117.8, 93.8)
- removed the VIA at (118.3, 93.8)
- removed the VIA at (118.8, 93.8)
- removed the VIA at (119.3, 93.8)
- removed the VIA at (119.8, 93.8)
- removed the VIA at (120.3, 93.8)
- removed the VIA at (120.8, 93.8)
- removed the VIA at (121.4, 93.2)
- removed the VIA at (121.1, 93.5)
- removed the VIA at (121.4, 92.7)
- removed the VIA at (125.0, 87.0)
- removed the VIA at (121.4, 92.2)
- removed the VIA at (121.4, 91.7)
- removed the VIA at (121.4, 91.2)
- removed the VIA at (121.4, 90.7)
- removed the VIA at (121.4, 90.2)
- removed the VIA at (121.4, 89.7)
- removed the VIA at (121.4, 89.2)
- removed the VIA at (121.4, 88.7)
- removed the VIA at (121.4, 88.2)
- removed the VIA at (121.4, 87.7)
- removed the VIA at (125.0, 89.6)
- removed the VIA at (121.4, 87.2)
- removed the VIA at (121.7, 86.9)
- removed the VIA at (122.1, 86.6)
- removed the VIA at (112.7, 92.5)
- removed the VIA at (112.7, 93.0)
- removed the VIA at (113.0, 93.2)
- removed the VIA at (113.5, 92.5)
- removed the VIA at (113.8, 92.6)
- removed the VIA at (113.3, 94.6)
- removed the VIA at (113.8, 94.6)
- removed the VIA at (114.3, 94.6)
- removed the VIA at (114.8, 94.6)
- removed the VIA at (115.3, 94.6)
- removed the VIA at (115.8, 94.6)
- removed the VIA at (116.3, 94.6)
- removed the VIA at (116.8, 94.6)
- removed the VIA at (117.3, 94.6)
- removed the VIA at (117.8, 94.6)
- removed the VIA at (118.3, 94.6)
- removed the VIA at (118.8, 94.6)
- removed the VIA at (128.0, 76.3)
- removed the VIA at (119.3, 94.6)
- removed the VIA at (119.8, 94.6)
- removed the VIA at (120.3, 94.6)
- removed the VIA at (120.8, 94.6)
- removed the VIA at (121.3, 94.6)
- removed the VIA at (122.2, 93.2)
- removed the VIA at (122.2, 93.7)
- removed the VIA at (121.9, 94.0)
- removed the VIA at (121.6, 94.3)
- removed the VIA at (122.2, 92.7)
- removed the VIA at (125.0, 76.3)
- removed the VIA at (122.2, 92.2)
- removed the VIA at (122.2, 91.7)
- removed the VIA at (122.2, 91.2)
- removed the VIA at (122.2, 90.7)
- removed the VIA at (122.2, 90.2)
- removed the VIA at (122.2, 89.7)
- removed the VIA at (122.2, 89.2)
- removed the VIA at (122.2, 88.7)
- removed the VIA at (122.2, 88.2)
- removed the VIA at (122.2, 87.7)
- added J10: Osc Power, EtherkitKicadLibrary:SIL-2, F.Cu at (103.9, 84.1)
- added VIA: VAL**, EtherkitKicadLibrary:VIA-05, F.Cu at (117.2, 90.5)
- added VIA: VAL**, EtherkitKicadLibrary:VIA-05, F.Cu at (117.2, 89.4)
- added VIA: VAL**, EtherkitKicadLibrary:VIA-05, F.Cu at (117.2, 88.3)
- added VIA: VAL**, EtherkitKicadLibrary:VIA-05, F.Cu at (117.6, 87.4)
- added VIA: VAL**, EtherkitKicadLibrary:VIA-05, F.Cu at (118.4, 86.7)
- added VIA: VAL**, EtherkitKicadLibrary:VIA-05, F.Cu at (114.7, 90.0)
- added VIA: VAL**, EtherkitKicadLibrary:VIA-05, F.Cu at (114.7, 88.9)
- added VIA: VAL**, EtherkitKicadLibrary:VIA-05, F.Cu at (114.7, 87.8)
- added VIA: VAL**, EtherkitKicadLibrary:VIA-05, F.Cu at (114.9, 86.8)
- added VIA: VAL**, EtherkitKicadLibrary:VIA-05, F.Cu at (115.7, 86.0)
- added VIA: VAL**, EtherkitKicadLibrary:VIA-05, F.Cu at (116.5, 85.3)
- added VIA: VAL**, EtherkitKicadLibrary:VIA-05, F.Cu at (117.1, 84.5)
- added VIA: VAL**, EtherkitKicadLibrary:VIA-05, F.Cu at (117.1, 83.3)
- added VIA: VAL**, EtherkitKicadLibrary:VIA-05, F.Cu at (117.1, 82.1)
- added VIA: VAL**, EtherkitKicadLibrary:VIA-05, F.Cu at (117.1, 80.8)
- added VIA: VAL**, EtherkitKicadLibrary:VIA-05, F.Cu at (117.1, 79.5)
- added VIA: VAL**, EtherkitKicadLibrary:VIA-05, F.Cu at (117.1, 78.2)
- added VIA: VAL**, EtherkitKicadLibrary:VIA-05, F.Cu at (117.1, 76.9)
- added VIA: VAL**, EtherkitKicadLibrary:VIA-05, F.Cu at (117.1, 75.6)
- added VIA: VAL**, EtherkitKicadLibrary:VIA-05, F.Cu at (117.1, 74.2)
- added VIA: VAL**, EtherkitKicadLibrary:VIA-05, F.Cu at (117.1, 72.8)
- added VIA: VAL**, EtherkitKicadLibrary:VIA-05, F.Cu at (117.1, 71.3)
- added VIA: VAL**, EtherkitKicadLibrary:VIA-05, F.Cu at (117.1, 69.8)
- added VIA: VAL**, EtherkitKicadLibrary:VIA-05, F.Cu at (117.1, 68.3)
- added VIA: VAL**, EtherkitKicadLibrary:VIA-05, F.Cu at (117.1, 67.0)
- added VIA: VAL**, EtherkitKicadLibrary:VIA-05, F.Cu at (117.1, 65.6)
- added VIA: VAL**, EtherkitKicadLibrary:VIA-05, F.Cu at (117.1, 64.3)
- added VIA: VAL**, EtherkitKicadLibrary:VIA-05, F.Cu at (117.3, 63.1)
- added VIA: VAL**, EtherkitKicadLibrary:VIA-05, F.Cu at (118.2, 62.4)
- added VIA: VAL**, EtherkitKicadLibrary:VIA-05, F.Cu at (114.6, 91.7)
- added VIA: VAL**, EtherkitKicadLibrary:VIA-05, F.Cu at (115.3, 91.0)
- added VIA: VAL**, EtherkitKicadLibrary:VIA-05, F.Cu at (115.8, 90.0)
- added VIA: VAL**, EtherkitKicadLibrary:VIA-05, F.Cu at (115.8, 88.9)
- added VIA: VAL**, EtherkitKicadLibrary:VIA-05, F.Cu at (115.8, 87.8)
- added VIA: VAL**, EtherkitKicadLibrary:VIA-05, F.Cu at (116.5, 86.8)
- added VIA: VAL**, EtherkitKicadLibrary:VIA-05, F.Cu at (117.3, 86.0)
- added VIA: VAL**, EtherkitKicadLibrary:VIA-05, F.Cu at (118.2, 85.2)
- added VIA: VAL**, EtherkitKicadLibrary:VIA-05, F.Cu at (119.2, 86.0)
- added VIA: VAL**, EtherkitKicadLibrary:VIA-05, F.Cu at (119.6, 84.8)
- added VIA: VAL**, EtherkitKicadLibrary:VIA-05, F.Cu at (118.3, 84.0)
- added VIA: VAL**, EtherkitKicadLibrary:VIA-05, F.Cu at (112.3, 92.7)
- added VIA: VAL**, EtherkitKicadLibrary:VIA-05, F.Cu at (118.3, 82.7)
- added VIA: VAL**, EtherkitKicadLibrary:VIA-05, F.Cu at (118.3, 81.3)
- added VIA: VAL**, EtherkitKicadLibrary:VIA-05, F.Cu at (118.3, 80.0)
- added VIA: VAL**, EtherkitKicadLibrary:VIA-05, F.Cu at (118.3, 78.8)
- added VIA: VAL**, EtherkitKicadLibrary:VIA-05, F.Cu at (118.3, 77.5)
- added VIA: VAL**, EtherkitKicadLibrary:VIA-05, F.Cu at (118.3, 76.3)
- added VIA: VAL**, EtherkitKicadLibrary:VIA-05, F.Cu at (118.3, 75.0)
- added VIA: VAL**, EtherkitKicadLibrary:VIA-05, F.Cu at (118.3, 73.5)
- added VIA: VAL**, EtherkitKicadLibrary:VIA-05, F.Cu at (118.3, 72.0)
- added VIA: VAL**, EtherkitKicadLibrary:VIA-05, F.Cu at (118.3, 70.5)
- added VIA: VAL**, EtherkitKicadLibrary:VIA-05, F.Cu at (113.3, 93.0)
- added VIA: VAL**, EtherkitKicadLibrary:VIA-05, F.Cu at (118.3, 69.0)
- added VIA: VAL**, EtherkitKicadLibrary:VIA-05, F.Cu at (118.3, 67.7)
- added VIA: VAL**, EtherkitKicadLibrary:VIA-05, F.Cu at (118.3, 66.2)
- added VIA: VAL**, EtherkitKicadLibrary:VIA-05, F.Cu at (118.3, 65.0)
- added VIA: VAL**, EtherkitKicadLibrary:VIA-05, F.Cu at (118.8, 63.9)
- added VIA: VAL**, EtherkitKicadLibrary:VIA-05, F.Cu at (119.6, 83.3)
- added VIA: VAL**, EtherkitKicadLibrary:VIA-05, F.Cu at (119.6, 82.0)
- added VIA: VAL**, EtherkitKicadLibrary:VIA-05, F.Cu at (119.6, 80.7)
- added VIA: VAL**, EtherkitKicadLibrary:VIA-05, F.Cu at (119.6, 79.4)
- added VIA: VAL**, EtherkitKicadLibrary:VIA-05, F.Cu at (111.0, 92.7)
- added VIA: VAL**, EtherkitKicadLibrary:VIA-05, F.Cu at (114.5, 93.0)
- added VIA: VAL**, EtherkitKicadLibrary:VIA-05, F.Cu at (111.3, 93.8)
- added VIA: VAL**, EtherkitKicadLibrary:VIA-05, F.Cu at (112.5, 94.2)
- added VIA: VAL**, EtherkitKicadLibrary:VIA-05, F.Cu at (113.8, 94.2)
- added VIA: VAL**, EtherkitKicadLibrary:VIA-05, F.Cu at (114.8, 94.2)
- added VIA: VAL**, EtherkitKicadLibrary:VIA-05, F.Cu at (116.1, 93.8)
- added VIA: VAL**, EtherkitKicadLibrary:VIA-05, F.Cu at (117.0, 93.1)
- added VIA: VAL**, EtherkitKicadLibrary:VIA-05, F.Cu at (117.8, 92.2)
- added VIA: VAL**, EtherkitKicadLibrary:VIA-05, F.Cu at (118.5, 91.2)
- added VIA: VAL**, EtherkitKicadLibrary:VIA-05, F.Cu at (118.5, 90.0)
- added VIA: VAL**, EtherkitKicadLibrary:VIA-05, F.Cu at (118.5, 88.8)
- added VIA: VAL**, EtherkitKicadLibrary:VIA-05, F.Cu at (115.6, 92.5)
- added VIA: VAL**, EtherkitKicadLibrary:VIA-05, F.Cu at (119.0, 87.9)
- added VIA: VAL**, EtherkitKicadLibrary:VIA-05, F.Cu at (116.5, 91.6)
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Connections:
- J4 pad 2: Net-(J4-Pad2) -> GND
- J5 pad 2: Net-(J5-Pad2) -> GND
- J6 pad 2: Net-(J6-Pad2) -> GND
- J7 pad 2: Net-(J4-Pad2) -> GND
- J8 pad 2: Net-(J5-Pad2) -> GND
- J9 pad 2: Net-(J6-Pad2) -> GND
- U2 pad 10: Net-(T1-Pad6) -> Net-(J4-Pad1)
- U2 pad 6: Net-(T3-Pad6) -> Net-(J6-Pad1)
- U2 pad 9: Net-(T2-Pad6) -> Net-(J5-Pad1)
- X1 pad 4: +3.3VREG -> Net-(J10-Pad2)
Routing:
- net Net-(T1-Pad6): track 37.1 -> 0.00 mm
- net Net-(T2-Pad6): track 28.9 -> 0.00 mm
- net Net-(J4-Pad1): track 10.9 -> 39.6 mm
- net Net-(J5-Pad2): track 21.4 -> 0.00 mm, vias 1 -> 0
- net Net-(J4-Pad2): track 21.3 -> 0.00 mm, vias 1 -> 0
- net Net-(J6-Pad2): track 21.3 -> 0.00 mm, vias 1 -> 0
- net Net-(T3-Pad6): track 20.9 -> 0.00 mm
- net Net-(J5-Pad1): track 10.9 -> 30.1 mm
- net Net-(J6-Pad1): track 10.9 -> 22.2 mm
- net Net-(J10-Pad2): track 0.00 -> 7.89 mm
- net +3.3VREG: track 72.0 -> 66.1 mm
- net Net-(Q2-Pad1): track 24.5 -> 29.2 mm, vias 2 -> 3
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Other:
- board size 40 x 50 mm -> 30 x 50 mm
- board text added: "Corr."
- board text added: "INT SEL"
- board text added: "OSC PWR"
- board text added: "Rev C"
- board text added: "etherkit.com 2015"
- board text removed: "INTF SEL"
- board text removed: "Rev B"
- board text removed: "etherkit.com 2014"
